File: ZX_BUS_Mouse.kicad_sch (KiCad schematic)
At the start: 29 parts, among them J1 X1A, J2 X1B, J3 Conn_02x30_Odd_Even, J4 Mini-DIN-6, J5 Conn_02x03_Odd_Even ISP, J6 Conn_01x04 Debug, J7 Conn_02x05_Odd_Even JTAG, U1 ATmega8A-A, U2 EPM3032ALC44, U3 AMS1117-3.3

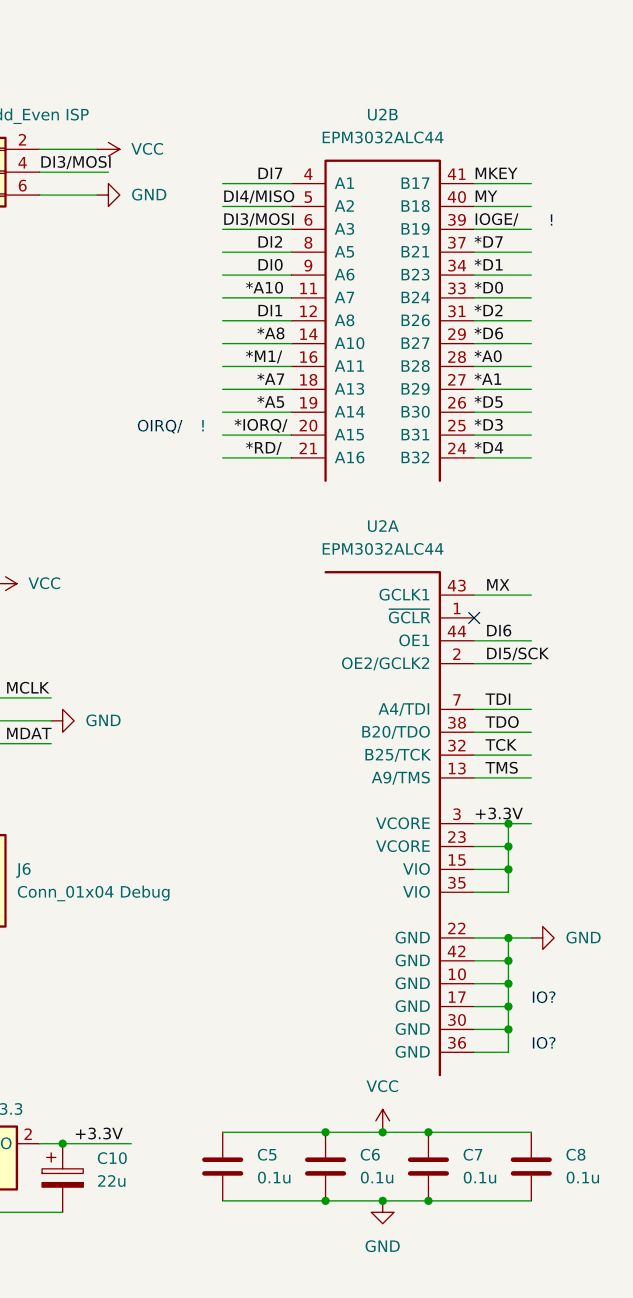
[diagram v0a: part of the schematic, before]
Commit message: Route PCB. Reassign EPM3032 IO pins.
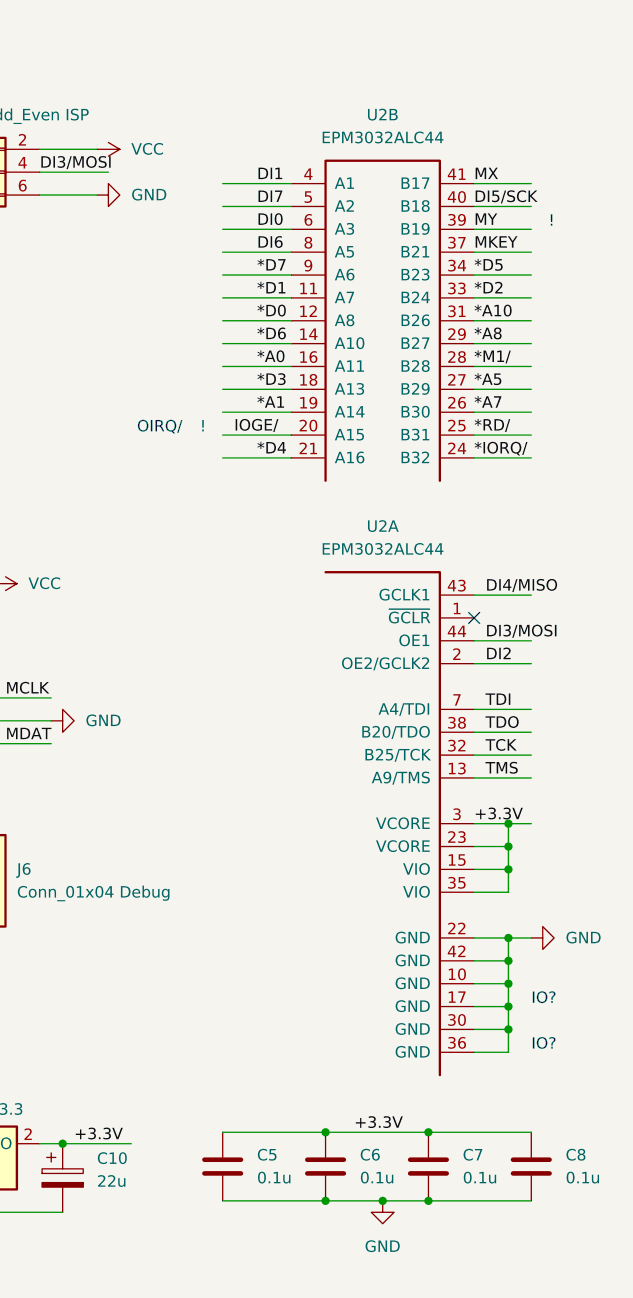
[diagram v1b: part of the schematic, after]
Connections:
- net *A0: now also U2.16 (A11); no longer U2.28 (B28)
- net *A1: now also U2.19 (A14); no longer U2.27 (B29)
- net *A10: now also U2.31 (B26); no longer U2.11 (A7)
- net *A5: now also U2.27 (B29); no longer U2.19 (A14)
- net *A7: now also U2.26 (B30); no longer U2.18 (A13)
- net *A8: now also U2.29 (B27); no longer U2.14 (A10)
- net *D0: now also U2.12 (A8); no longer U2.33 (B24)
- net *D1: now also U2.11 (A7); no longer U2.34 (B23)
- net *D2: now also U2.33 (B24); no longer U2.31 (B26)
- net *D3: now also U2.18 (A13); no longer U2.25 (B31)
- net *D4: now also U2.21 (A16); no longer U2.24 (B32)
- net *D5: now also U2.34 (B23); no longer U2.26 (B30)
- net *D6: now also U2.14 (A10); no longer U2.29 (B27)
- net *D7: now also U2.9 (A6); no longer U2.37 (B21)
- net *IORQ/: now also U2.24 (B32); no longer U2.20 (A15)
- net *M1/: now also U2.28 (B28); no longer U2.16 (A11)
- net *RD/: now also U2.25 (B31); no longer U2.21 (A16)
- net +3.3V: now also C5.1, C6.1, C7.1, C8.1
- net DI0: now also U2.6 (A3); no longer U2.9 (A6)
- net DI1: now also U2.4 (A1); no longer U2.12 (A8)
- net DI2: now also U2.2 (OE2/GCLK2); no longer U2.8 (A5)
- net DI3/MOSI: now also U2.44 (OE1); no longer U2.6 (A3)
- net DI4/MISO: now also U2.43 (GCLK1); no longer U2.5 (A2)
- net DI5/SCK: now also U2.40 (B18); no longer U2.2 (OE2/GCLK2)
- net DI6: now also U2.8 (A5); no longer U2.44 (OE1)
- net DI7: now also U2.5 (A2); no longer U2.4 (A1)
- net IOGE/: now also U2.20 (A15); no longer U2.39 (B19)
- net MKEY: now also U2.37 (B21); no longer U2.41 (B17)
- net MX: now also U2.41 (B17); no longer U2.43 (GCLK1)
- net MY: now also U2.39 (B19); no longer U2.40 (B18)
- net VCC: no longer C5.1, C6.1, C7.1, C8.1

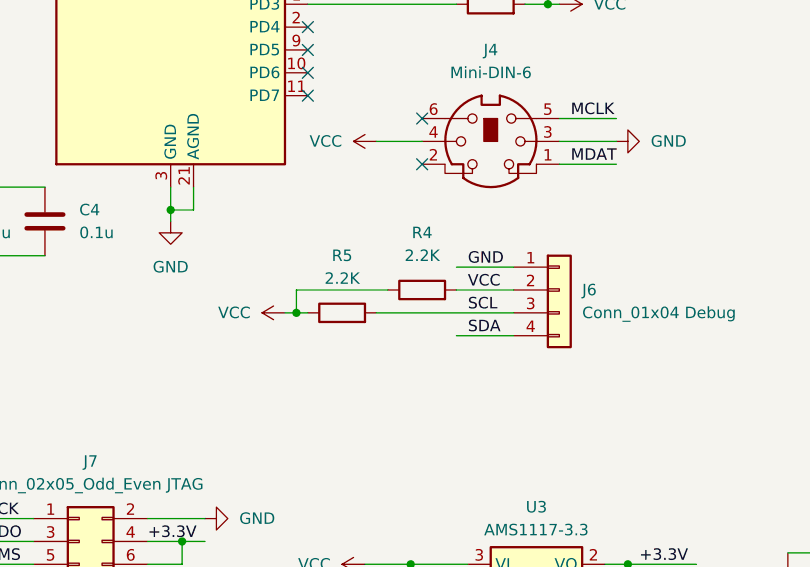
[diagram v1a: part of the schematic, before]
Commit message: Correct SDA pullup resistor.
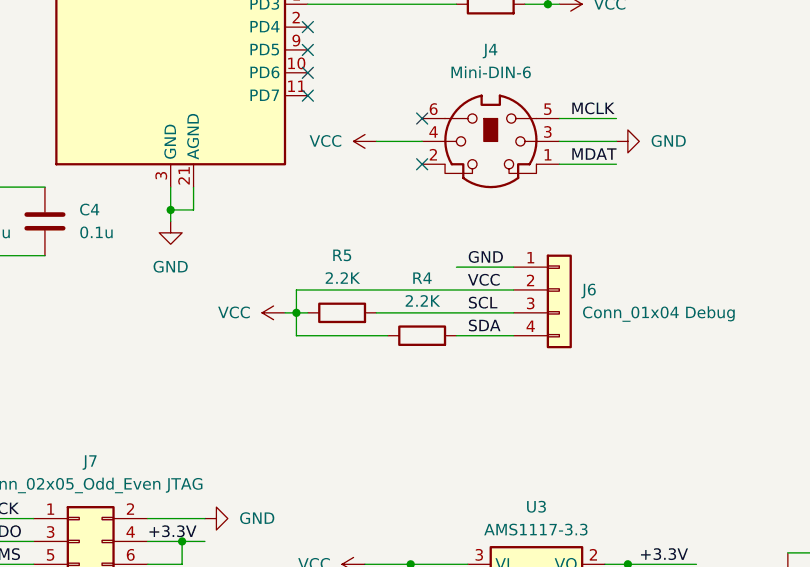
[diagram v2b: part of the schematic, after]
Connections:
- net SDA: now also R4.2
- net VCC: no longer R4.2
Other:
- moved on the sheet: R4
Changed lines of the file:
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@@
-    (stroke (width 0) (type default))
-  )
-  (wire (pts (xy 187.96 115.57) (xy 194.31 115.57))
     (stroke (width 0) (type default))
   )
@@
     (stroke (width 0) (type default))
   )
-  (wire (pts (xy 180.34 115.57) (xy 170.18 115.57))
+  (wire (pts (xy 180.34 120.65) (xy 170.18 120.65))
     (stroke (width 0) (type default))
   )
@@
     (stroke (width 0) (type default))
   )
+  (wire (pts (xy 170.18 115.57) (xy 170.18 118.11))
+    (stroke (width 0) (type default))
+  )
   (wire (pts (xy 50.8 52.07) (xy 59.69 52.07))
     (stroke (width 0) (type default))
@@
     (stroke (width 0) (type default))
   )
+  (wire (pts (xy 194.31 115.57) (xy 170.18 115.57))
+    (stroke (width 0) (type default))
+  )
   (wire (pts (xy 184.15 38.1) (xy 191.77 38.1))
     (stroke (width 0) (type default))
@@
     (stroke (width 0) (type default))
   )
-  (wire (pts (xy 170.18 115.57) (xy 170.18 118.11))
+  (wire (pts (xy 170.18 120.65) (xy 170.18 118.11))
     (stroke (width 0) (type default))
   )
@@
     )
   )
-  (symbol (lib_id "Device:R") (at 184.15 115.57 90) (unit 1)
+  (symbol (lib_id "Device:R") (at 184.15 120.65 90) (unit 1)
     (in_bom yes) (on_board no) (dnp no) (fields_autoplaced)
-    (property "Reference" "R4" (at 184.15 109.22 90)
-      (effects (font (size 1.27 1.27)))
-    )
-    (property "Value" "2.2K" (at 184.15 111.76 90)
-      (effects (font (size 1.27 1.27)))
-    )
-    (property "Footprint" "Resistor_SMD:R_1206_3216Metric_Pad1.30x1.75mm_HandSolder" (at 184.15 117.348 90)
-      (effects (font (size 1.27 1.27)) hide)
-    )
-    (property "Datasheet" "~" (at 184.15 115.57 0)
-      (effects (font (size 1.27 1.27)) hide)
-    )
+    (property "Reference" "R4" (at 184.15 114.3 90)
+      (effects (font (size 1.27 1.27)))
+    )
+    (property "Value" "2.2K" (at 184.15 116.84 90)
+      (effects (font (size 1.27 1.27)))
+    )
+    (property "Footprint" "Resistor_SMD:R_1206_3216Metric_Pad1.30x1.75mm_HandSolder" (at 184.15 122.428 90)
+      (effects (font (size 1.27 1.27)) hide)
+    )
+    (property "Datasheet" "~" (at 184.15 120.65 0)
+      (effects (font (size 1.27 1.27)) hide)
+    )

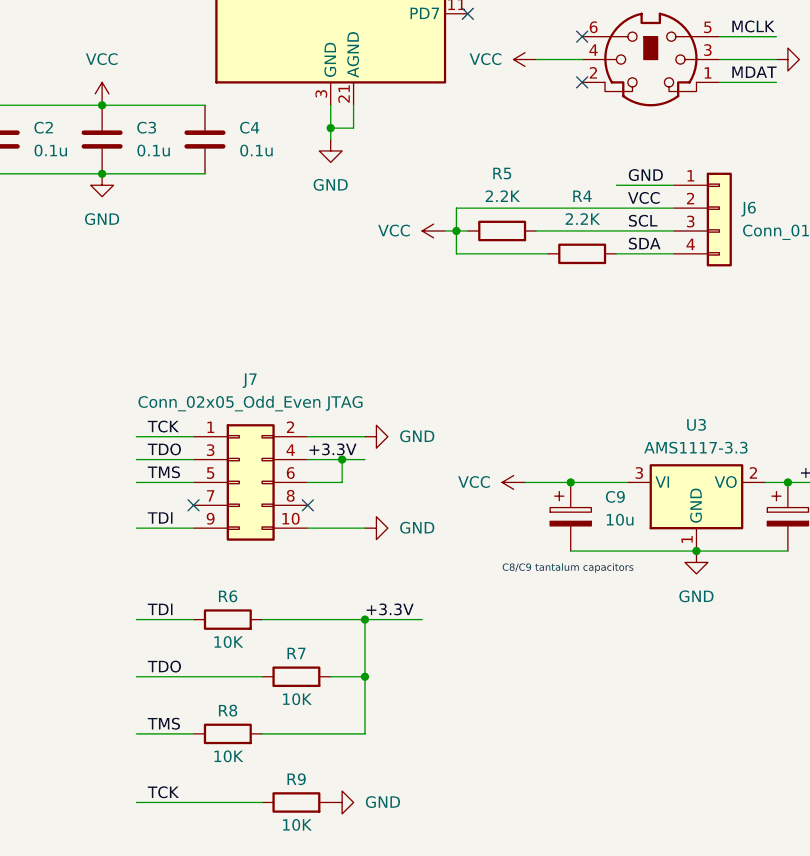
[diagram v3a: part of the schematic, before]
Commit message: Arrange resistors references.
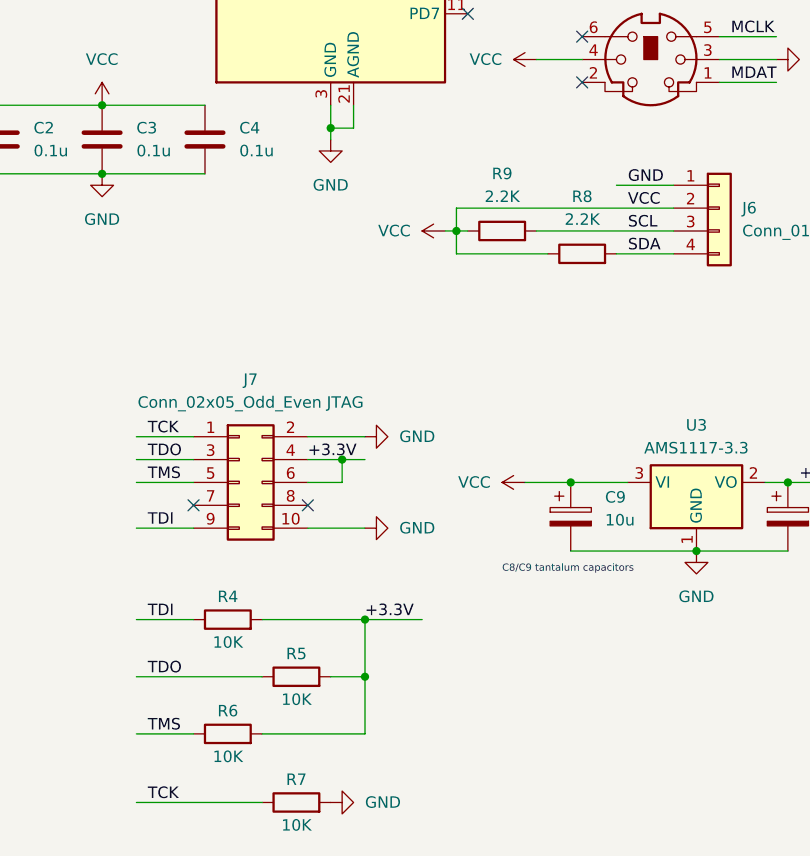
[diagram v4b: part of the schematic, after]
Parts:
- renumbered R6 to R4, R7 to R5, R8 to R6, R9 to R7, R4 to R8, R5 to R9
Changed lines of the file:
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@@
   (symbol (lib_id "Device:R") (at 144.78 161.29 90) (unit 1)
     (in_bom yes) (on_board yes) (dnp no)
-    (property "Reference" "R6" (at 144.78 158.75 90)
+    (property "Reference" "R4" (at 144.78 158.75 90)
       (effects (font (size 1.27 1.27)))
     )
@@
       (project "ZX_BUS_Mouse"
         (path "/3450efc4-f02c-4d95-a19b-bf60e75dcf1f"
-          (reference "R6") (unit 1)
+          (reference "R4") (unit 1)
         )
       )
@@
   (symbol (lib_id "Device:R") (at 175.26 118.11 90) (unit 1)
     (in_bom yes) (on_board yes) (dnp no) (fields_autoplaced)
-    (property "Reference" "R5" (at 175.26 111.76 90)
+    (property "Reference" "R9" (at 175.26 111.76 90)
       (effects (font (size 1.27 1.27)))
     )
@@
       (project "ZX_BUS_Mouse"
         (path "/3450efc4-f02c-4d95-a19b-bf60e75dcf1f"
-          (reference "R5") (unit 1)
+          (reference "R9") (unit 1)
         )
       )
@@
   (symbol (lib_id "Device:R") (at 184.15 120.65 90) (unit 1)
     (in_bom yes) (on_board yes) (dnp no) (fields_autoplaced)
-    (property "Reference" "R4" (at 184.15 114.3 90)
+    (property "Reference" "R8" (at 184.15 114.3 90)
       (effects (font (size 1.27 1.27)))
     )
@@
       (project "ZX_BUS_Mouse"
         (path "/3450efc4-f02c-4d95-a19b-bf60e75dcf1f"
-          (reference "R4") (unit 1)
+          (reference "R8") (unit 1)
         )
       )
@@
   (symbol (lib_id "Device:R") (at 152.4 181.61 90) (unit 1)
     (in_bom yes) (on_board yes) (dnp no)
-    (property "Reference" "R9" (at 152.4 179.07 90)
+    (property "Reference" "R7" (at 152.4 179.07 90)
       (effects (font (size 1.27 1.27)))
     )
@@
       (project "ZX_BUS_Mouse"
         (path "/3450efc4-f02c-4d95-a19b-bf60e75dcf1f"
-          (reference "R9") (unit 1)
+          (reference "R7") (unit 1)
         )
       )
@@
   (symbol (lib_id "Device:R") (at 152.4 167.64 90) (unit 1)
     (in_bom yes) (on_board yes) (dnp no)
-    (property "Reference" "R7" (at 152.4 165.1 90)
+    (property "Reference" "R5" (at 152.4 165.1 90)
       (effects (font (size 1.27 1.27)))
     )
@@
       (project "ZX_BUS_Mouse"
         (path "/3450efc4-f02c-4d95-a19b-bf60e75dcf1f"
-          (reference "R7") (unit 1)
+          (reference "R5") (unit 1)
         )
       )
@@
   (symbol (lib_id "Device:R") (at 144.78 173.99 90) (unit 1)
     (in_bom yes) (on_board yes) (dnp no)
-    (property "Reference" "R8" (at 144.78 171.45 90)
+    (property "Reference" "R6" (at 144.78 171.45 90)
       (effects (font (size 1.27 1.27)))
     )
@@
       (project "ZX_BUS_Mouse"
         (path "/3450efc4-f02c-4d95-a19b-bf60e75dcf1f"
-          (reference "R8") (unit 1)
-        )
-      )
+          (reference "R6") (unit 1)
+        )
+      )

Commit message: Remove unused 2x30 connector from PCB.
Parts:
- removed J3: Conn_02x30_Odd_Even, my_lib:PinSocket_2x30_P2.54mm_Vertical, symbol Connector_Generic:Conn_02x30_Odd_Even
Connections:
- no-connect marks 17 -> 53
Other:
- note removed: "!"
- note removed: "OIRQ/"
- moved on the sheet: C1, C10, C2, C3, C4, C5, C6, C7, C8, C9, J1, J2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

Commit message: Rename libs/my_lib.pretty libs/zx_bus.pretty.
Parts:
- J1, J2: footprint my_lib:PinSocket_1x31_P2.54mm_2 -> zx_bus:PinSocket_1x31_P2.54mm_2
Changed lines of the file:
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@@
       (effects (font (size 1.27 1.27)))
     )
-    (property "Footprint" "my_lib:PinSocket_1x31_P2.54mm_2" (at 181.61 63.5 0)
+    (property "Footprint" "zx_bus:PinSocket_1x31_P2.54mm_2" (at 181.61 63.5 0)
       (effects (font (size 1.27 1.27)) hide)
     )
@@
       (effects (font (size 1.27 1.27)))
     )
-    (property "Footprint" "my_lib:PinSocket_1x31_P2.54mm_2" (at 209.55 63.5 0)
-      (effects (font (size 1.27 1.27)) hide)
-    )
+    (property "Footprint" "zx_bus:PinSocket_1x31_P2.54mm_2" (at 209.55 63.5 0)
+      (effects (font (size 1.27 1.27)) hide)
+    )
